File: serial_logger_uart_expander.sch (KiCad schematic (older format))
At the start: 56 parts, among them J1 CN6, J2 CN8, J3 CN5, J4 CN9, J5 Screw_Terminal_01x10, J6 Screw_Terminal_01x10, U1 M74HC4851, U10 2N7002PS, U11 2N7002PS, U12 2N7002PS, U13 2N7002PS, U14 ESDA17-5SC6, U15 NRF24L01_Breakout, U2 M74HC4851, U3 ESDA17-5SC6, U4 ESDA17-5SC6, U5 ESDA17-5SC6, U6 2N7002PS, U7 2N7002PS, U8 2N7002PS, U9 2N7002PS

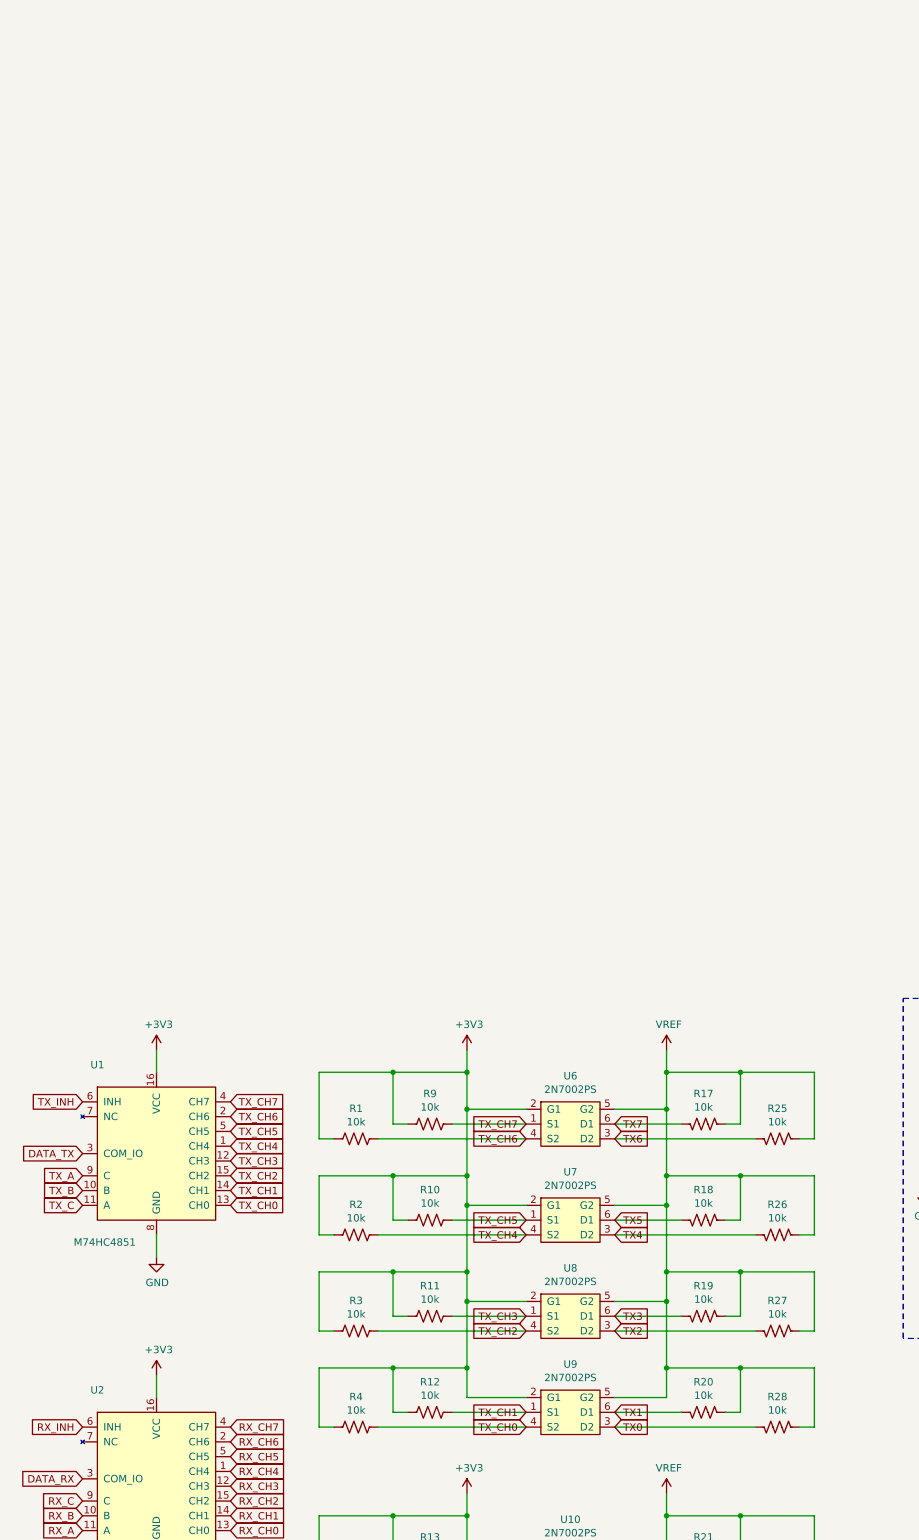
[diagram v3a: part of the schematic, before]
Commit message: started updating mosfets to 2n7002
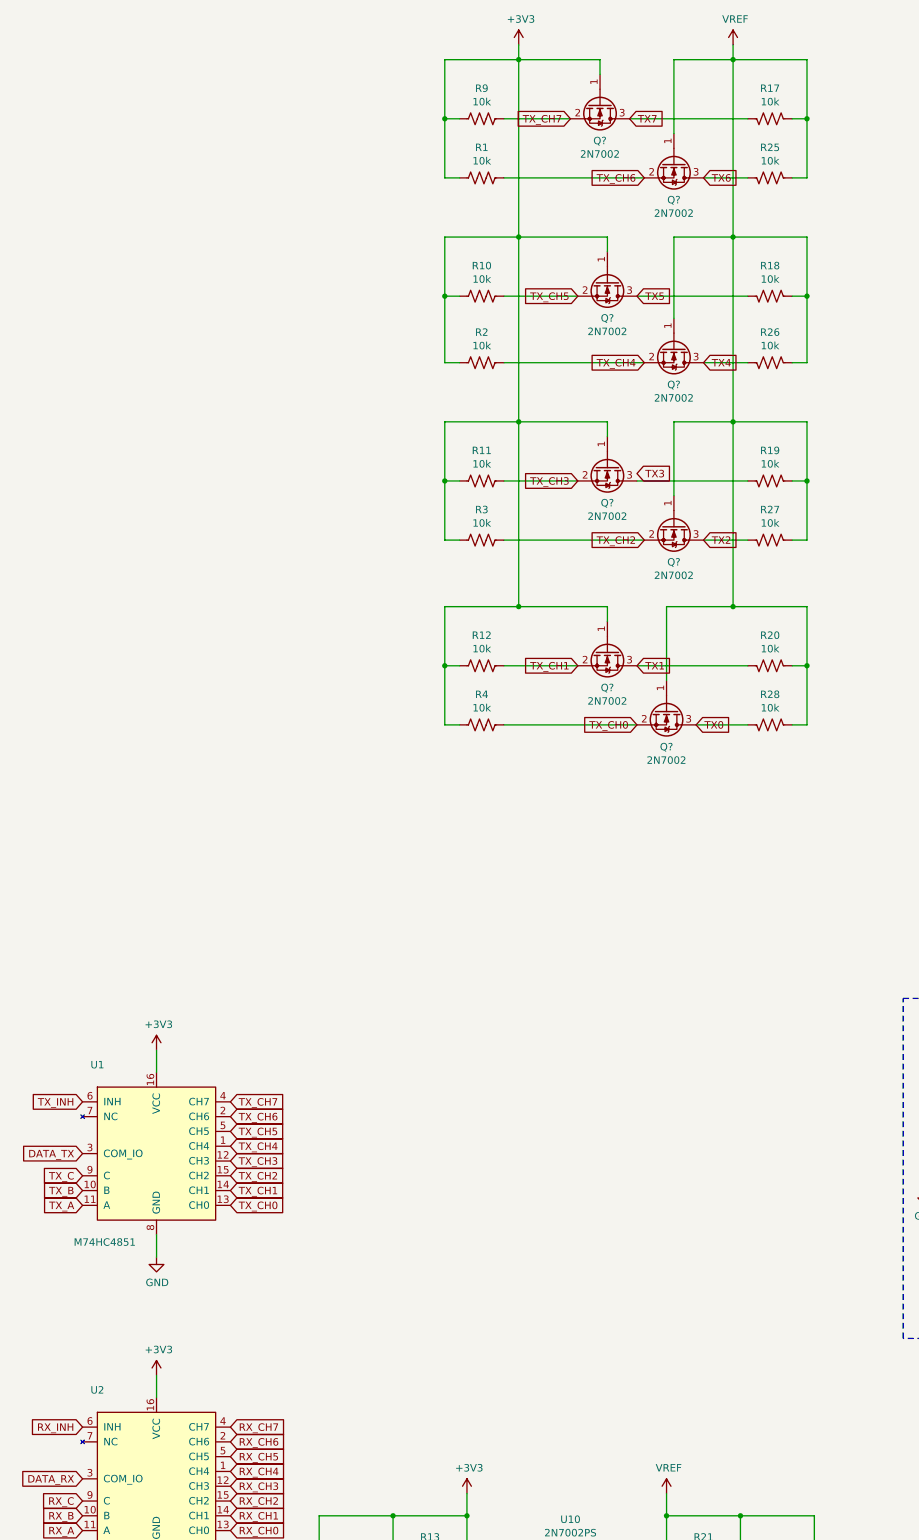
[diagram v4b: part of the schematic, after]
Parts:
- removed U6, U7, U8, U9: 2N7002PS, my_lib:2N7002PS_NEXPERA_SOT-363, symbol my_lib:2N7002PS
- added Q? (x8): 2N7002, Package_TO_SOT_SMD:SOT-23, symbol Transistor_FET:2N7002
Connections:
- net +3V3: now also Q?.1 (G), Q?.1 (G), Q?.1 (G), Q?.1 (G)
- net TX0: now also Q?.3 (D)
- net TX1: now also Q?.3 (D)
- net TX2: now also Q?.3 (D)
- net TX3: no longer R19.2
- net TX4: now also Q?.3 (D)
- net TX5: now also Q?.3 (D)
- net TX6: now also Q?.3 (D)
- net TX7: now also Q?.3 (D)
- net TX_A: now also U1.11 (A); no longer U1.9 (C)
- net TX_C: now also U1.9 (C); no longer U1.11 (A)
- net TX_CH0: now also Q?.2 (S)
- net TX_CH1: now also Q?.2 (S)
- net TX_CH2: now also Q?.2 (S)
- net TX_CH3: now also Q?.2 (S)
- net TX_CH4: now also Q?.2 (S)
- net TX_CH5: now also Q?.2 (S)
- net TX_CH6: now also Q?.2 (S)
- net TX_CH7: now also Q?.2 (S)
- net VBUS: now also Q?.1 (G), Q?.1 (G), Q?.1 (G), Q?.1 (G)
- new net: Q?.3 (D), R19.2
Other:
- moved on the sheet: R1, R10, R11, R12, R17, R18, R19, R2, R20, R25, R26, R27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

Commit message: completed v0.1 design with 2n7002; no BOM or gerbers
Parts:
- removed U10, U11, U12, U13: 2N7002PS, my_lib:2N7002PS_NEXPERA_SOT-363, symbol my_lib:2N7002PS
- added Q1, Q2, Q3, Q4, Q5, Q6, Q7, Q8: 2N7002, Package_TO_SOT_SMD:SOT-23, symbol Transistor_FET:2N7002
- gave numbers to parts that had none: 8
- renumbered J5 to J1, J1 to J2, J2 to J3, J3 to J4, J4 to J5, R13 to R1, R29 to R10, R22 to R11, R30 to R12, R23 to R13, R31 to R14, R24 to R15, R32 to R16, R9 to R17, R1 to R18, R10 to R19, R5 to R2, R2 to R20, R11 to R21, R3 to R22, R12 to R23, R4 to R24, R17 to R25, R25 to R26, R18 to R27, R26 to R28, R19 to R29, R14 to R3, R27 to R30, R20 to R31, R28 to R32, R6 to R4, R15 to R5, R7 to R6, R16 to R7, R21 to R9, U15 to U3, U3 to U4, U4 to U5, U5 to U6, U14 to U7
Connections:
- net +3V3: now also Q1.1 (G), Q2.1 (G), Q3.1 (G), Q4.1 (G)
- net RX0: now also Q8.3 (D)
- net RX1: now also Q4.3 (D)
- net RX2: now also Q7.3 (D)
- net RX3: now also Q3.3 (D)
- net RX4: now also Q6.3 (D)
- net RX5: now also Q2.3 (D)
- net RX6: now also Q5.3 (D)
- net RX7: now also Q1.3 (D)
- net RX_CH0: now also Q8.2 (S)
- net RX_CH1: now also Q4.2 (S)
- net RX_CH2: now also Q7.2 (S)
- net RX_CH3: now also Q3.2 (S)
- net RX_CH4: now also Q6.2 (S)
- net RX_CH5: now also Q2.2 (S)
- net RX_CH6: now also Q5.2 (S)
- net RX_CH7: now also Q1.2 (S)
- net TX3: now also Q11.3 (D), R29.2
- net VBUS: now also Q5.1 (G), Q6.1 (G), Q7.1 (G), Q8.1 (G)
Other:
- note added: "RX LEVEL SHIFTER"
- note added: "TX LEVEL SHIFTER"
- note removed: "VGS MAX = +/- 20V"
- moved on the sheet: C1, J1, J2, J3, J4, J5, J6, Q10, Q11, Q12, Q13, Q14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
